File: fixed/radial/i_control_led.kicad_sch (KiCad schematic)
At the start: 14 parts, among them J1 Conn_01x04, J2 Conn_01x04, Q1 MMBT5551L, U1 LM2775DSG, U2 LMV321

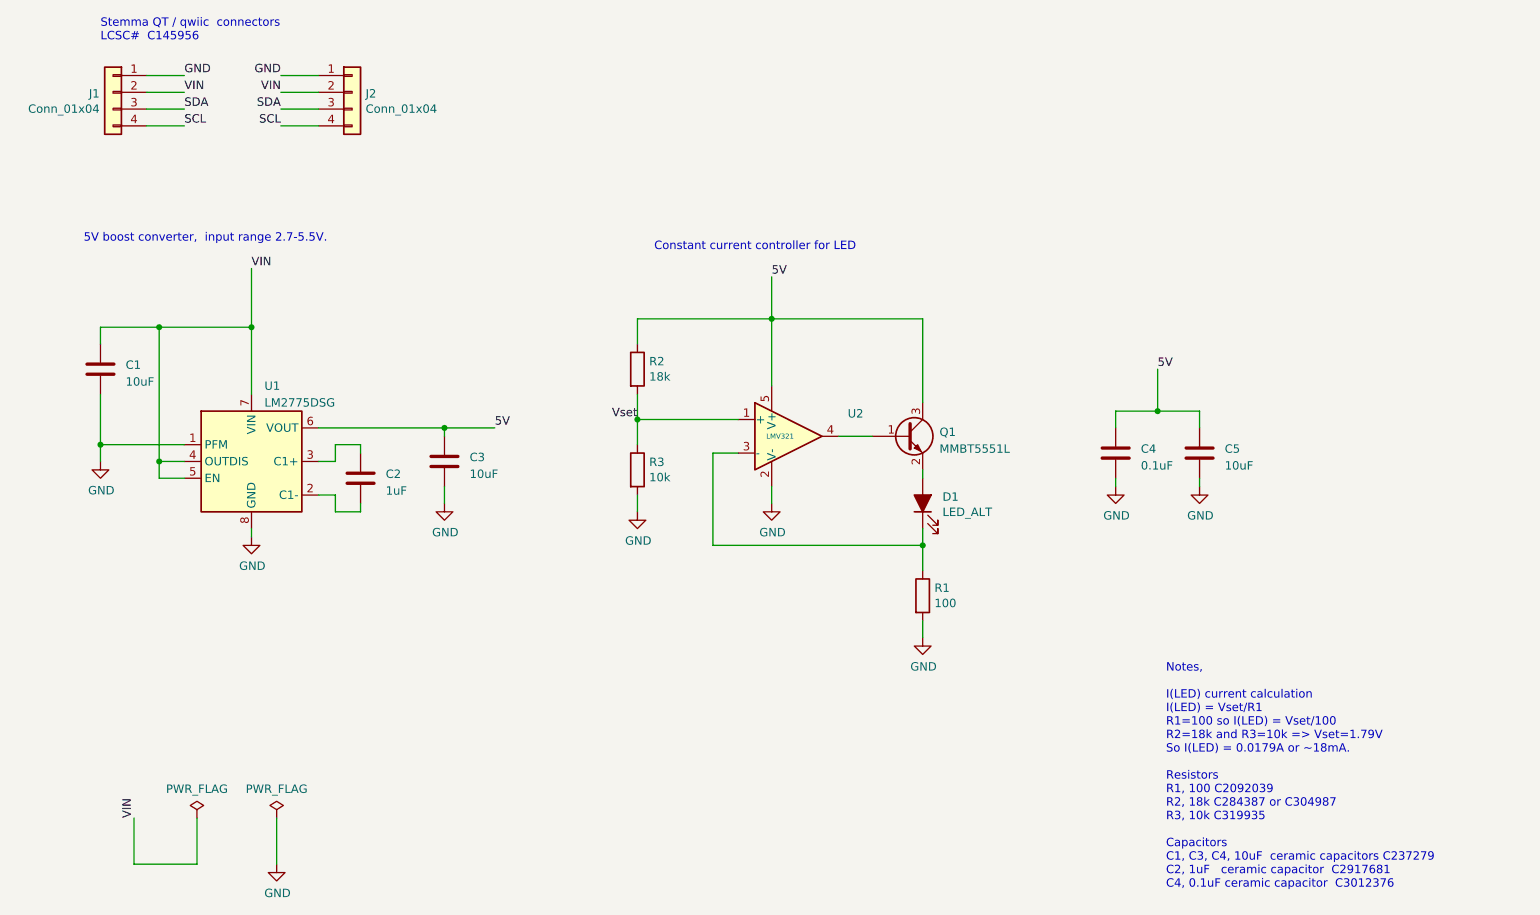
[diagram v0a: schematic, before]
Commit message: Added fixed current radial led design.
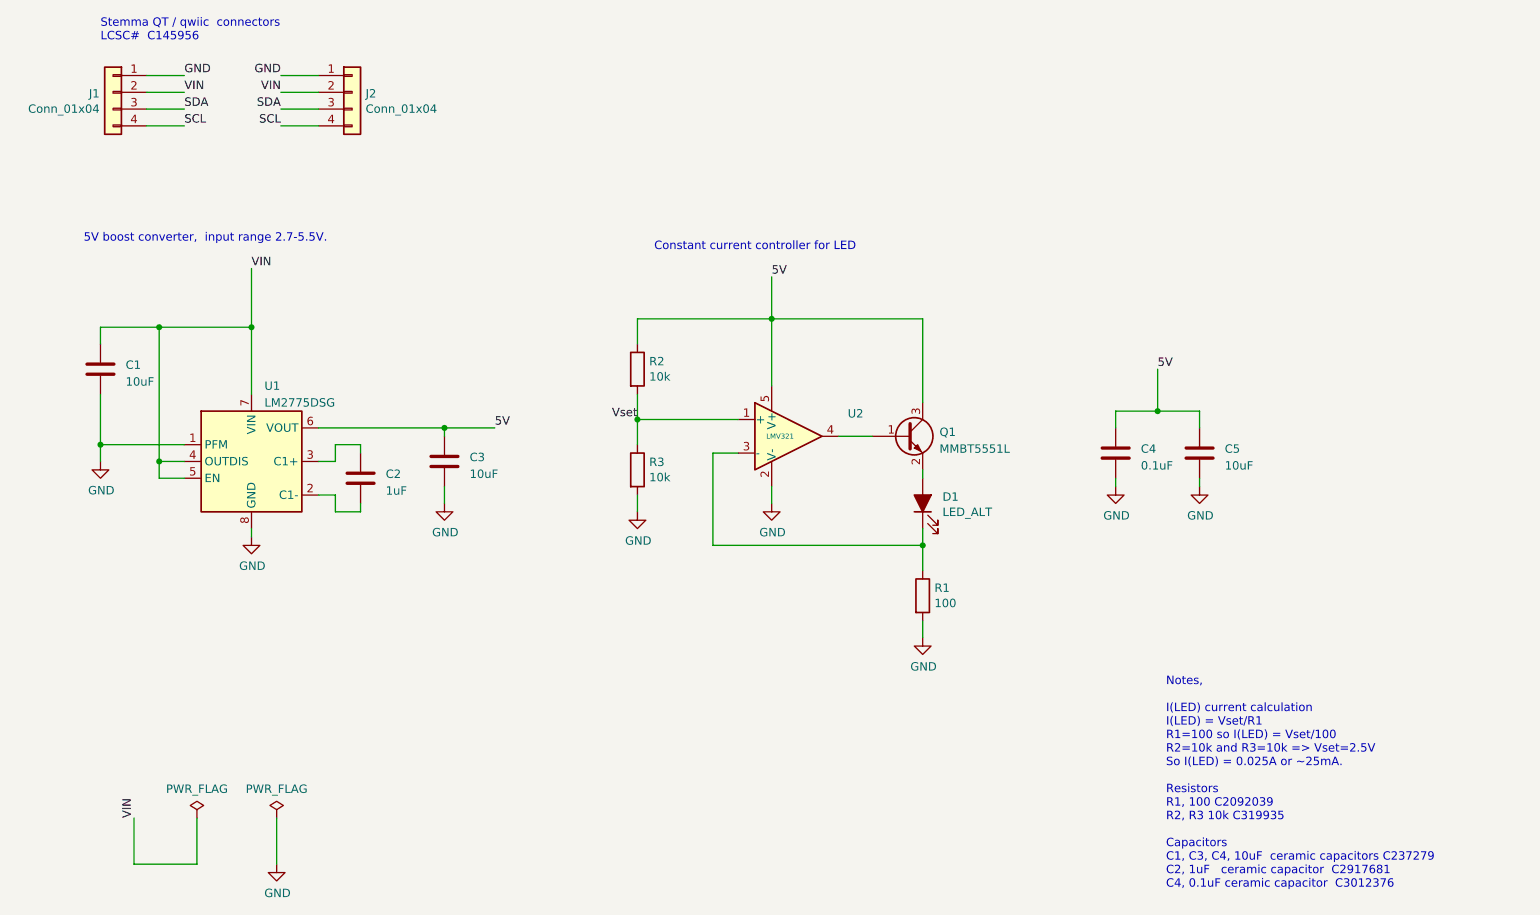
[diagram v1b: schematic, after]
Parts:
- D1: footprint LED_SMD:LED_0603_1608Metric -> LED_THT:LED_D3.0mm
- R2: value 18k -> 10k
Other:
- note added: "Notes, I(LED) current calculation I(LED) = Vset/R1 R1=100 so I(LED) = Vset/100 R2=10k and R3=10k => Vset=2.5V So I(LED) = 0.025A or ~25mA. Resistors R1, 100 C2092039 R2, R3 10k C319935 Capacitors C1, C3, C4, 10uF ceramic capacitors C237279 C2, 1uF ceramic capacitor C2917681 C4, 0.1uF ceramic capacitor C3012376"
- note removed: "Notes, I(LED) current calculation I(LED) = Vset/R1 R1=100 so I(LED) = Vset/100 R2=18k and R3=10k => Vset=1.79V So I(LED) = 0.0179A or ~18mA. Resistors R1, 100 C2092039 R2, 18k C284387 or C304987 R3, 10k C319935 Capacitors C1, C3, C4, 10uF ceramic capacitors C237279 C2, 1uF ceramic capacitor C2917681 C4, 0.1uF ceramic capacitor C3012376"
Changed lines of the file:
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@@
     (effects (font (size 1.27 1.27)) (justify left bottom))
   )
-  (text "Notes, \n\nI(LED) current calculation\nI(LED) = Vset/R1\nR1=100 so I(LED) = Vset/100\nR2=18k and R3=10k => Vset=1.79V\nSo I(LED) = 0.0179A or ~18mA. \n\nResistors\nR1, 100 C2092039\nR2, 18k C284387 or C304987\nR3, 10k C319935\n\nCapacitors\nC1, C3, C4, 10uF  ceramic capacitors C237279\nC2, 1uF   ceramic capacitor  C2917681\nC4, 0.1uF ceramic capacitor  C3012376\n"
+  (text "Notes, \n\nI(LED) current calculation\nI(LED) = Vset/R1\nR1=100 so I(LED) = Vset/100\nR2=10k and R3=10k => Vset=2.5V\nSo I(LED) = 0.025A or ~25mA. \n\nResistors\nR1, 100 C2092039\nR2, R3 10k C319935\n\nCapacitors\nC1, C3, C4, 10uF  ceramic capacitors C237279\nC2, 1uF   ceramic capacitor  C2917681\nC4, 0.1uF ceramic capacitor  C3012376\n"
     (at 198.12 154.94 0)
     (effects (font (size 1.27 1.27)) (justify left bottom))
@@
       (effects (font (size 1.27 1.27)) (justify right))
     )
-    (property "Footprint" "LED_SMD:LED_0603_1608Metric" (at 161.29 96.52 0)
+    (property "Footprint" "LED_THT:LED_D3.0mm" (at 161.29 96.52 0)
       (effects (font (size 1.27 1.27)) hide)
     )
@@
       (effects (font (size 1.27 1.27)) (justify left))
     )
-    (property "Value" "18k" (at 119.888 77.343 0)
-      (effects (font (size 1.27 1.27)) (justify left))
-    )
+    (property "Value" "10k" (at 119.888 77.343 0)
+      (effects (font (size 1.27 1.27)) (justify left))
+    )
